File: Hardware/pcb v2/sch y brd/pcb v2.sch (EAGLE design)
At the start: 61 parts, among them J1 AVR_SPI_PRG_6PTH, J2 1981584-1, J3 HDMI, J4 HDMI, Q1 PMBT3904, Q2 PMBT3904, Q4 MC-306, U1 ATMEGA328P, U2 TXS0108EPWR-TSSOP20, U3 MB85RS16N, U4 ADP3338AKCZ-3.3RL7, U5 DS1307SO8, U6 BATTERYBATTERY1225_SMT, Y2 CSTCE16M0V53-R0 16MHZ

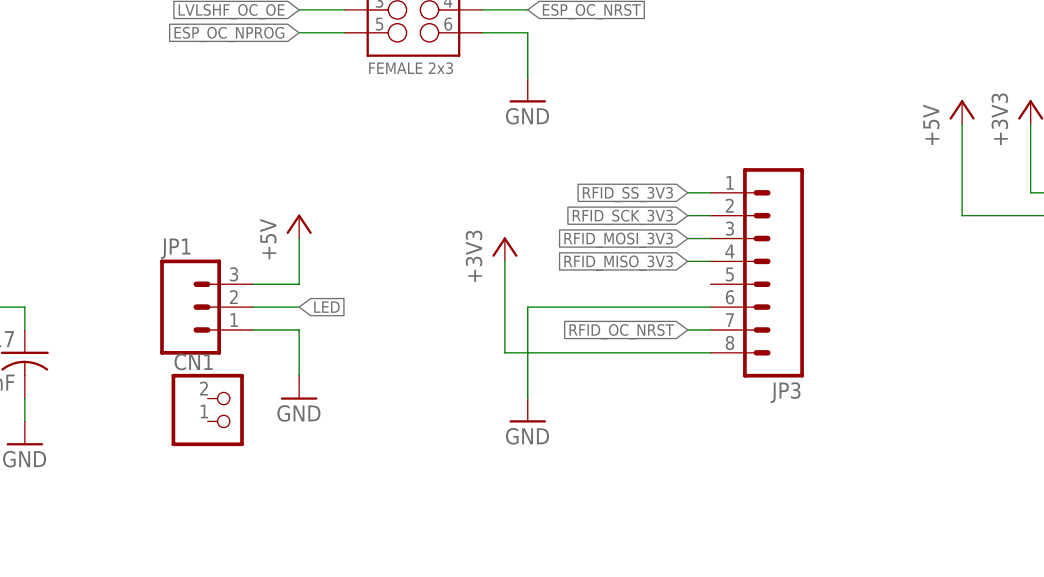
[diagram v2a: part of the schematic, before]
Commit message: posiciones componentes externos
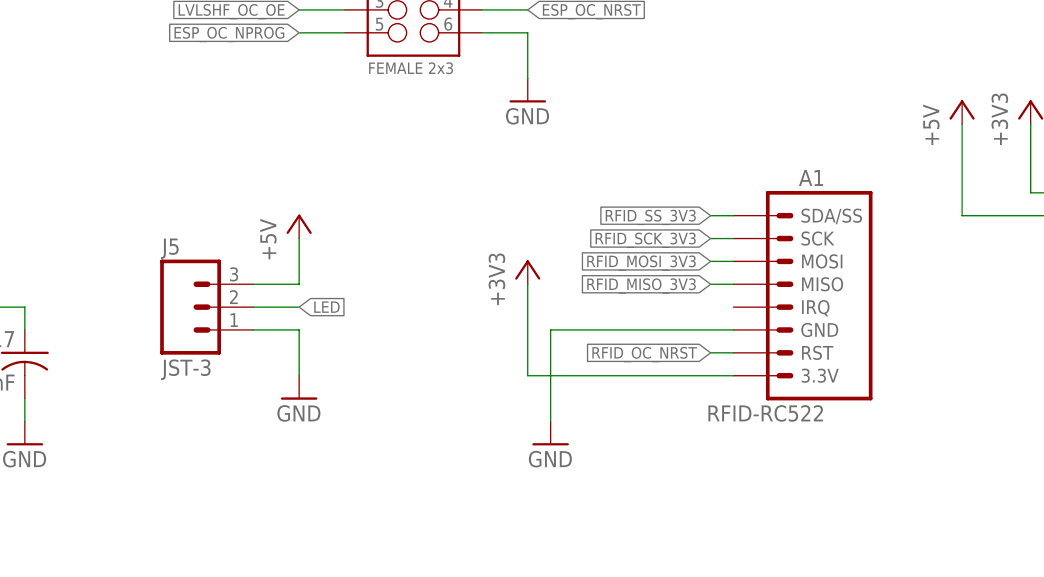
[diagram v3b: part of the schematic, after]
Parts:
- removed CN1: (no value), adafruit:JST_2PIN-SMT
- removed JP1: (no value), SparkFun-Connectors:M03JST-SMD
- removed JP3: (no value), SparkFun-Connectors:M081X08
- added A1: RFID-RC522, partes v2:RFID-RC522
- added J5: JST-3, partes v2:JST-3
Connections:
- net +3V3: now also A1.3.3V; no longer JP3.8
- net +5V: now also J5.3; no longer JP1.3
- net GND: now also A1.GND, J5.1; no longer JP1.1, JP3.6
- net LED: now also J5.2; no longer JP1.2
- net RFID_MISO_3V3: now also A1.MISO; no longer JP3.4
- net RFID_MOSI_3V3: now also A1.MOSI; no longer JP3.3
- net RFID_OC_NRST: now also A1.RST; no longer JP3.7
- net RFID_SCK_3V3: now also A1.SCK; no longer JP3.2
- net RFID_SS_3V3: now also A1.SDA/SS; no longer JP3.1
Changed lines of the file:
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@@
 <setting verticaltext="up"/>
 </settings>
-<grid distance="0.1" unitdist="inch" unit="inch" style="dots" multiple="1" display="yes" altdistance="0.01" altunitdist="inch" altunit="inch"/>
+<grid distance="0.1" unitdist="inch" unit="inch" style="lines" multiple="1" display="no" altdistance="0.01" altunitdist="inch" altunit="inch"/>
 <layers>
 <layer number="1" name="Top" color="4" fill="1" visible="no" active="no"/>
@@
 <part name="C19" library="rcl" deviceset="C-US" device="C0805" value="1uF"/>
 <part name="GND20" library="supply1" deviceset="GND" device=""/>
-<part name="JP3" library="SparkFun-Connectors" deviceset="M08" device="1X08"/>
-<part name="GND19" library="supply1" deviceset="GND" device=""/>
-<part name="+3V37" library="supply1" deviceset="+3V3" device=""/>
 <part name="U2" library="Seeed-IC-2016" deviceset="LOGIC-TXS0108EPWR(TSSOP20)" device="" value="TXS0108EPWR-TSSOP20"/>
 <part name="P+4" library="supply1" deviceset="+5V" device=""/>
@@
 <part name="P+8" library="supply1" deviceset="+5V" device=""/>
 <part name="+3V38" library="supply1" deviceset="+3V3" device=""/>
-<part name="JP1" library="SparkFun-Connectors" deviceset="M03" device="JST-SMD"/>
 <part name="P+6" library="supply1" deviceset="+5V" device=""/>
 <part name="GND17" library="supply1" deviceset="GND" device=""/>
@@
 <part name="C16" library="rcl" deviceset="CPOL-US" device="UD-5X5,8"/>
 <part name="SP1" library="adafruit" deviceset="SPEAKER" device="/PS12"/>
-<part name="CN1" library="adafruit" deviceset="JST_2PIN" device="-SMT"/>
+<part name="J5" library="partes v2" deviceset="JST-3" device=""/>
+<part name="A1" library="partes v2" deviceset="RFID-RC522" device=""/>
+<part name="+3V1" library="supply1" deviceset="+3V3" device=""/>
+<part name="GND27" library="supply1" deviceset="GND" device=""/>
 </parts>
 <sheets>
@@
 <instance part="C19" gate="G$1" x="365.76" y="114.3"/>
 <instance part="GND20" gate="1" x="365.76" y="104.14"/>
-<instance part="JP3" gate="G$1" x="368.3" y="15.24" rot="R180"/>
-<instance part="GND19" gate="1" x="342.9" y="-2.54"/>
-<instance part="+3V37" gate="G$1" x="340.36" y="17.78"/>
 <instance part="U2" gate="G$1" x="193.04" y="20.32" smashed="yes" rot="MR0">
 <attribute name="NAME" x="201.93" y="34.29" size="1.27" layer="95" ratio="10" rot="MR0"/>
@@
 <instance part="P+8" gate="1" x="391.16" y="33.02"/>
 <instance part="+3V38" gate="G$1" x="398.78" y="33.02"/>
-<instance part="JP1" gate="G$1" x="304.8" y="10.16"/>
 <instance part="P+6" gate="1" x="317.5" y="20.32"/>
 <instance part="GND17" gate="1" x="317.5" y="0"/>
@@
 <attribute name="VALUE" x="400.685" y="115.57" size="1.778" layer="96" rot="R270"/>
 </instance>
-<instance part="CN1" gate="G$1" x="309.88" y="-2.54"/>
+<instance part="J5" gate="G$1" x="304.8" y="10.16"/>
+<instance part="A1" gate="G$1" x="373.38" y="12.7" rot="MR0"/>
+<instance part="+3V1" gate="G$1" x="342.9" y="15.24"/>
+<instance part="GND27" gate="1" x="345.44" y="-5.08"/>
 </instances>
 <busses>
@@
 <wire x1="365.76" y1="109.22" x2="365.76" y2="106.68" width="0.1524" layer="91"/>
 <pinref part="GND20" gate="1" pin="GND"/>
-</segment>
-<segment>
-<pinref part="JP3" gate="G$1" pin="6"/>
-<wire x1="363.22" y1="10.16" x2="342.9" y2="10.16" width="0.1524" layer="91"/>
-<wire x1="342.9" y1="10.16" x2="342.9" y2="0" width="0.1524" layer="91"/>
-<pinref part="GND19" gate="1" pin="GND"/>
 </segment>
 <segment>
@@
 </segment>
 <segment>
-<pinref part="JP1" gate="G$1" pin="1"/>
 <wire x1="312.42" y1="7.62" x2="317.5" y2="7.62" width="0.1524" layer="91"/>
 <wire x1="317.5" y1="7.62" x2="317.5" y2="2.54" width="0.1524" layer="91"/>
 <pinref part="GND17" gate="1" pin="GND"/>
+<pinref part="J5" gate="G$1" pin="1"/>
 </segment>
 <segment>
@@
 <wire x1="337.82" y1="40.64" x2="342.9" y2="40.64" width="0.1524" layer="91"/>
 <wire x1="342.9" y1="40.64" x2="342.9" y2="35.56" width="0.1524" layer="91"/>
+</segment>
+<segment>
+<pinref part="GND27" gate="1" pin="GND"/>
+<pinref part="A1" gate="G$1" pin="GND"/>
+<wire x1="345.44" y1="-2.54" x2="345.44" y2="7.62" width="0.1524" layer="91"/>
+<wire x1="345.44" y1="7.62" x2="365.76" y2="7.62" width="0.1524" layer="91"/>
 </segment>
 </net>
@@
 </segment>
 <segment>
-<pinref part="JP1" gate="G$1" pin="3"/>
 <wire x1="312.42" y1="12.7" x2="317.5" y2="12.7" width="0.1524" layer="91"/>
 <wire x1="317.5" y1="12.7" x2="317.5" y2="17.78" width="0.1524" layer="91"/>
 <pinref part="P+6" gate="1" pin="+5V"/>
+<pinref part="J5" gate="G$1" pin="3"/>
 </segment>
 <segment>
@@
 </segment>
 <segment>
-<pinref part="JP1" gate="G$1" pin="2"/>
 <wire x1="312.42" y1="10.16" x2="317.5" y2="10.16" width="0.1524" layer="91"/>
 <label x="317.5" y="10.16" size="1.27" layer="95" xref="yes"/>
+<pinref part="J5" gate="G$1" pin="2"/>
 </segment>
 </net>
@@
 <net name="RFID_MISO_3V3" class="0">
 <segment>
-<pinref part="JP3" gate="G$1" pin="4"/>
-<wire x1="363.22" y1="15.24" x2="360.68" y2="15.24" width="0.1524" layer="91"/>
-<label x="360.68" y="15.24" size="1.27" layer="95" rot="R180" xref="yes"/>
-</segment>
-<segment>
 <pinref part="U2" gate="G$1" pin="A4"/>
 <wire x1="205.74" y1="20.32" x2="228.6" y2="20.32" width="0.1524" layer="91"/>
@@
 <junction x="228.6" y="20.32"/>
 </segment>
+<segment>
+<pinref part="A1" gate="G$1" pin="MISO"/>
+<wire x1="365.76" y1="12.7" x2="363.22" y2="12.7" width="0.1524" layer="91"/>
+<label x="363.22" y="12.7" size="1.27" layer="95" rot="R180" xref="yes"/>
+</segment>
 </net>
 <net name="RFID_MOSI_3V3" class="0">
-<segment>
-<pinref part="JP3" gate="G$1" pin="3"/>
-<wire x1="363.22" y1="17.78" x2="360.68" y2="17.78" width="0.1524" layer="91"/>
-<label x="360.68" y="17.78" size="1.27" layer="95" rot="R180" xref="yes"/>
-</segment>
 <segment>
 <pinref part="U2" gate="G$1" pin="A3"/>
@@
 <junction x="226.06" y="22.86"/>
 </segment>
+<segment>
+<pinref part="A1" gate="G$1" pin="MOSI"/>
+<wire x1="365.76" y1="15.24" x2="363.22" y2="15.24" width="0.1524" layer="91"/>
+<label x="363.22" y="15.24" size="1.27" layer="95" rot="R180" xref="yes"/>
+</segment>
 </net>
 <net name="RFID_SCK_3V3" class="0">
-<segment>
-<pinref part="JP3" gate="G$1" pin="2"/>
-<wire x1="363.22" y1="20.32" x2="360.68" y2="20.32" width="0.1524" layer="91"/>
-<label x="360.68" y="20.32" size="1.27" layer="95" rot="R180" xref="yes"/>
-</segment>
 <segment>
 <pinref part="U2" gate="G$1" pin="A2"/>
@@
 <junction x="223.52" y="25.4"/>
 </segment>
+<segment>
+<pinref part="A1" gate="G$1" pin="SCK"/>
+<wire x1="365.76" y1="17.78" x2="363.22" y2="17.78" width="0.1524" layer="91"/>
+<label x="363.22" y="17.78" size="1.27" layer="95" rot="R180" xref="yes"/>
+</segment>
 </net>
 <net name="RFID_SS_3V3" class="0">
-<segment>
-<pinref part="JP3" gate="G$1" pin="1"/>
-<wire x1="363.22" y1="22.86" x2="360.68" y2="22.86" width="0.1524" layer="91"/>
-<label x="360.68" y="22.86" size="1.27" layer="95" rot="R180" xref="yes"/>
-</segment>
 <segment>
 <pinref part="U2" gate="G$1" pin="A1"/>
@@
 <label x="231.14" y="27.94" size="1.27" layer="95" xref="yes"/>
 </segment>
+<segment>
+<pinref part="A1" gate="G$1" pin="SDA/SS"/>
+<wire x1="365.76" y1="20.32" x2="363.22" y2="20.32" width="0.1524" layer="91"/>
+<label x="363.22" y="20.32" size="1.27" layer="95" rot="R180" xref="yes"/>
+</segment>
 </net>
 <net name="RFID_OC_NRST" class="0">
-<segment>
-<pinref part="JP3" gate="G$1" pin="7"/>
-<wire x1="363.22" y1="7.62" x2="360.68" y2="7.62" width="0.1524" layer="91"/>
-<label x="360.68" y="7.62" size="1.27" layer="95" rot="R180" xref="yes"/>
-</segment>
 <segment>
 <pinref part="U1" gate="G$1" pin="PD7(AIN1)"/>
@@
 <label x="121.92" y="50.8" size="1.27" layer="95" xref="yes"/>
 </segment>
+<segment>
+<pinref part="A1" gate="G$1" pin="RST"/>
+<wire x1="365.76" y1="5.08" x2="363.22" y2="5.08" width="0.1524" layer="91"/>
+<label x="363.22" y="5.08" size="1.27" layer="95" rot="R180" xref="yes"/>
+</segment>
 </net>
 <net name="+3V3" class="0">
-<segment>
-<pinref part="JP3" gate="G$1" pin="8"/>
-<wire x1="363.22" y1="5.08" x2="340.36" y2="5.08" width="0.1524" layer="91"/>
-<wire x1="340.36" y1="5.08" x2="340.36" y2="15.24" width="0.1524" layer="91"/>
-<pinref part="+3V37" gate="G$1" pin="+3V3"/>
-</segment>
 <segment>
 <pinref part="+3V34" gate="G$1" pin="+3V3"/>
@@
 <wire x1="398.78" y1="22.86" x2="414.02" y2="22.86" width="0.1524" layer="91"/>
 </segment>
+<segment>
+<pinref part="A1" gate="G$1" pin="3.3V"/>
+<wire x1="365.76" y1="2.54" x2="342.9" y2="2.54" width="0.1524" layer="91"/>
+<wire x1="342.9" y1="2.54" x2="342.9" y2="12.7" width="0.1524" layer="91"/>
+<pinref part="+3V1" gate="G$1" pin="+3V3"/>
+</segment>
 </net>
 <net name="N$8" class="0">
@@
 </schematic>
 </drawing>
+<compatibility>
+<note version="6.3" minversion="6.2.2" severity="warning">
+Since Version 6.2.2 text objects can contain more than one line,
+which will not be processed correctly with this version.
+</note>
+</compatibility>
 </eagle>
